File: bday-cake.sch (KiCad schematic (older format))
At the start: 3 parts

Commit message: update layout
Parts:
- added S1: SWITCH-TACTILE-SPST-NO-0.05A-24V-SMT-FSMSMTR, Wickerlib:SWITCH-TECONN-MOMENTARY-SMD-FSMSM, symbol wickerlib:SWITCH-TACTILE-SPST-NO-0.05A-24V-SMT-FSMSMTR
- R1: footprint Resistor_THT:R_Axial_DIN0207_L6.3mm_D2.5mm_P2.54mm_Vertical -> Resistor_THT:R_Axial_DIN0207_L6.3mm_D2.5mm_P7.62mm_Horizontal
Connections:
- net labels added: +3V3, GND
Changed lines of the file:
@@
 F 0 "R1" V 4993 2200 50  0000 C CNN
 F 1 "R" V 5084 2200 50  0000 C CNN
-F 2 "Resistor_THT:R_Axial_DIN0207_L6.3mm_D2.5mm_P2.54mm_Vertical" V 5130 2200 50  0001 C CNN
+F 2 "Resistor_THT:R_Axial_DIN0207_L6.3mm_D2.5mm_P7.62mm_Horizontal" V 5130 2200 50  0001 C CNN
 F 3 "~" H 5200 2200 50  0001 C CNN
 	1    5200 2200
@@
 	5050 2200 4600 2200
 Wire Wire Line
-	4600 2200 4600 2800
+	5650 2800 5650 2200
 Wire Wire Line
-	4600 2800 5200 2800
+	5200 2800 4600 2800
 Wire Wire Line
 	5400 2800 5650 2800
+$Comp
+L power:GND #PWR0101
+U 1 1 5E264F45
+P 4600 2800
+F 0 "#PWR0101" H 4600 2550 50  0001 C CNN
+F 1 "GND" H 4605 2627 50  0000 C CNN
+F 2 "" H 4600 2800 50  0001 C CNN
+F 3 "" H 4600 2800 50  0001 C CNN
+	1    4600 2800
+	1    0    0    -1
+$EndComp
+$Comp
+L power:+3V3 #PWR0102
+U 1 1 5E266A09
+P 5650 2800
+F 0 "#PWR0102" H 5650 2650 50  0001 C CNN
+F 1 "+3V3" V 5665 2928 50  0000 L CNN
+F 2 "" H 5650 2800 50  0001 C CNN
+F 3 "" H 5650 2800 50  0001 C CNN
+	1    5650 2800
+	0    1    1    0
+$EndComp
+Connection ~ 5650 2800
+$Comp
+L wickerlib:SWITCH-TACTILE-SPST-NO-0.05A-24V-SMT-FSMSMTR S1
+U 1 1 5E26A03A
+P 4600 2450
+F 0 "S1" V 4504 2555 50  0000 L CNN
+F 1 "SWITCH-TACTILE-SPST-NO-0.05A-24V-SMT-FSMSMTR" V 4595 2555 50  0000 L CNN
+F 2 "Wickerlib:SWITCH-TECONN-MOMENTARY-SMD-FSMSM" H 4600 2100 50  0001 C CIN
+F 3 "http://www.te.com/commerce/DocumentDelivery/DDEController?Action=srchrtrv&DocNm=1437566-3&DocType=Customer+Drawing&DocLang=English" H 4600 2450 5   0001 C CNN
+F 4 "SWITCH TACTILE SPST-NO 0.05A 24V" H 4600 2100 50  0001 C CIN "Description"
+F 5 "TE Conn" H 4600 2100 50  0001 C CIN "MF_Name"
+F 6 "FSMSMTR" H 4600 2100 50  0001 C CIN "MF_PN"
+F 7 "Digikey" H 4600 2100 50  0001 C CIN "S1_Name"
+F 8 "450-1758-1-ND" H 4600 2100 50  0001 C CIN "S1_PN"
+F 9 "461" H 4600 2100 50  0001 C CIN "XSize_mils"
+F 10 "154" H 4600 2100 50  0001 C CIN "YSize_mils"
+F 11 "smt" H 4600 2100 50  0001 C CIN "Type"
+	1    4600 2450
+	0    1    1    0
+$EndComp
 Wire Wire Line
-	5650 2800 5650 2200
+	4600 2600 4600 2800
+Connection ~ 4600 2800
 $EndSCHEMATC

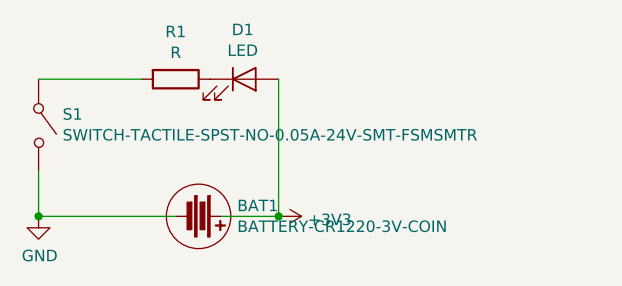
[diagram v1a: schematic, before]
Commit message: update schematic and layout
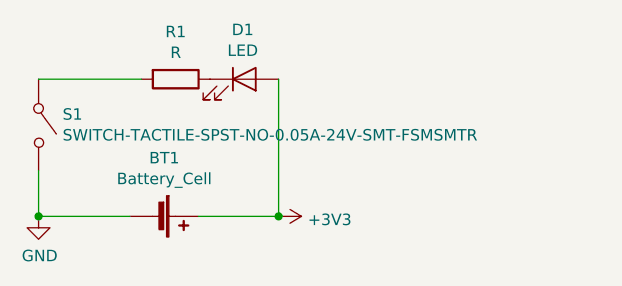
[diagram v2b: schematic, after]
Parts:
- removed BAT1: BATTERY-CR1220-3V-COIN, Wickerlib:BATT-HOLDER-CR1220-BK-916, symbol wickerlib:BATTERY-CR1220-3V-COIN
- added BT1: Battery_Cell, Battery:BatteryHolder_Keystone_3002_1x2032, symbol Device:Battery_Cell
- S1: footprint Wickerlib:SWITCH-TECONN-MOMENTARY-SMD-FSMSM -> Wickerlib:SWITCH-ESWITCH-SLIDE-TH-EG1218
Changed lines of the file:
@@
 	1    0    0    -1
-$EndComp
-$Comp
-L wickerlib:BATTERY-CR1220-3V-COIN BAT1
-U 1 1 5E246271
-P 5300 2800
-F 0 "BAT1" V 5254 2969 50  0000 L CNN
-F 1 "BATTERY-CR1220-3V-COIN" V 5345 2969 50  0000 L CNN
-F 2 "Wickerlib:BATT-HOLDER-CR1220-BK-916" H 5300 2450 50  0001 C CIN
-F 3 "http://www.memoryprotectiondevices.com/datasheets/BK-916-datasheet.pdf" H 5300 2800 5   0001 C CNN
-F 4 "BATTERY CR1220 3V COIN CELL" H 5300 2450 50  0001 C CIN "Description"
-F 5 "Panasonic" H 5300 2450 50  0001 C CIN "MF_Name"
-F 6 "CR1220" H 5300 2450 50  0001 C CIN "MF_PN"
-F 7 "Digikey" H 5300 2450 50  0001 C CIN "S1_Name"
-F 8 "P033-ND" H 5300 2450 50  0001 C CIN "S1_PN"
-F 9 "490" H 5300 2450 50  0001 C CIN "XSize_mils"
-F 10 "490" H 5300 2450 50  0001 C CIN "YSize_mils"
-F 11 "dnp" H 5300 2450 50  0001 C CIN "Type"
-	1    5300 2800
-	0    1    1    0
 $EndComp
 Wire Wire Line
@@
 Wire Wire Line
 	5650 2800 5650 2200
-Wire Wire Line
-	5200 2800 4600 2800
-Wire Wire Line
-	5400 2800 5650 2800
 $Comp
 L power:GND #PWR0101
@@
 	0    1    1    0
 $EndComp
-Connection ~ 5650 2800
 $Comp
 L wickerlib:SWITCH-TACTILE-SPST-NO-0.05A-24V-SMT-FSMSMTR S1
@@
 F 0 "S1" V 4504 2555 50  0000 L CNN
 F 1 "SWITCH-TACTILE-SPST-NO-0.05A-24V-SMT-FSMSMTR" V 4595 2555 50  0000 L CNN
-F 2 "Wickerlib:SWITCH-TECONN-MOMENTARY-SMD-FSMSM" H 4600 2100 50  0001 C CIN
+F 2 "Wickerlib:SWITCH-ESWITCH-SLIDE-TH-EG1218" H 4600 2100 50  0001 C CIN
 F 3 "http://www.te.com/commerce/DocumentDelivery/DDEController?Action=srchrtrv&DocNm=1437566-3&DocType=Customer+Drawing&DocLang=English" H 4600 2450 5   0001 C CNN
 F 4 "SWITCH TACTILE SPST-NO 0.05A 24V" H 4600 2100 50  0001 C CIN "Description"
@@
 Wire Wire Line
 	4600 2600 4600 2800
+$Comp
+L Device:Battery_Cell BT1
+U 1 1 5E26FE72
+P 5100 2800
+F 0 "BT1" V 4845 2850 50  0000 C CNN
+F 1 "Battery_Cell" V 4936 2850 50  0000 C CNN
+F 2 "Battery:BatteryHolder_Keystone_3002_1x2032" V 5100 2860 50  0001 C CNN
+F 3 "~" V 5100 2860 50  0001 C CNN
+	1    5100 2800
+	0    1    1    0
+$EndComp
+Wire Wire Line
+	5300 2800 5650 2800
+Connection ~ 5650 2800
+Wire Wire Line
+	5000 2800 4600 2800
 Connection ~ 4600 2800
 $EndSCHEMATC
